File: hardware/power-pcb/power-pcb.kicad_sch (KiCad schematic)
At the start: 28 parts, among them J1 MicroFit3.0_1x2, J2 XT60PW-M-AS, J3 XT30, J4 XT30, K1 CB1-P-12V, Q1 SI4946CDY-T1-GE3, Q2 IRF4905, U1 LTC4365TS8, U2 TMCS1100A2QDR

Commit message: Added power pcb sch + design
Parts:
- removed C1, C8: 100n, Capacitor_SMD:C_0805_2012Metric_Pad1.18x1.45mm_HandSolder, symbol Device:C_Small
- removed D1: 1N4007, Diode_THT:D_DO-41_SOD81_P10.16mm_Horizontal, symbol Diode:1N4007
- removed D2: 1N4744A, Diode_THT:D_DO-41_SOD81_P10.16mm_Horizontal, symbol Diode:1N47xxA
- removed HS1: Heatsink_Pad_2Pin, Project:265118ABHE22, symbol Mechanical:Heatsink_Pad_2Pin
- removed J1: MicroFit3.0_1x2, Project:Molex_Micro-Fit_3.0_43650-0215_1x02_P3.00mm_Vertical, symbol Connector_Generic:Conn_01x02
- removed K1: CB1-P-12V, Project:CB1P12V, symbol Relay:Relay_SPDT
- removed Q1: SI4946CDY-T1-GE3, Package_SO:SO-8_3.9x4.9mm_P1.27mm, symbol Project:SISB46DN-T1-GE3
- removed Q2: IRF4905, Package_TO_SOT_THT:TO-220-3_Vertical, symbol Transistor_FET:IRF4905
- removed R2, R79: 10k, Resistor_SMD:R_0805_2012Metric_Pad1.20x1.40mm_HandSolder, symbol Device:R
- removed R6: 100R, Resistor_SMD:R_0805_2012Metric_Pad1.20x1.40mm_HandSolder, symbol Device:R_Small
- removed R88: 1.5k, Resistor_SMD:R_0805_2012Metric_Pad1.20x1.40mm_HandSolder, symbol Device:R
- removed U2: TMCS1100A2QDR, Project:TMCS1100A2QDR, symbol Project:TMCS1100A2QDR
- added C1: 2200u_LowZ, Capacitor_THT:CP_Radial_D16.0mm_P7.50mm, symbol Device:C_Polarized
- added C2: 100n, Capacitor_SMD:C_0805_2012Metric_Pad1.18x1.45mm_HandSolder, symbol Device:C_Small
- added C3, C4: 10u, Capacitor_SMD:C_0805_2012Metric_Pad1.18x1.45mm_HandSolder, symbol Device:C_Small
- added H1, H2, H3, H4: MountingHole, MountingHole:MountingHole_3.2mm_M3, symbol Mechanical:MountingHole
- added J2: XT30, Project:AMASS_XT30UPB-M_1x02_P5.0mm_Vertical, symbol Connector_Generic:Conn_01x02
- added J3: MicroFit2x12_Odd_Even, Project:Molex_Micro-Fit_3.0_43045-2412_2x12_P3.00mm_Vertical, symbol Connector_Generic:Conn_02x12_Top_Bottom
- added J4: MicroFit2x12_CouterClockwise, Project:Molex_Micro-Fit_3.0_43045-2412_2x12_P3.00mm_Vertical, symbol Connector_Generic:Conn_02x12_Counter_Clockwise
- added J7: XT60PW-M-AS, Connector_AMASS:AMASS_XT60-M_1x02_P7.20mm_Vertical, symbol Connector_Generic:Conn_01x02
- added J8: JST_XH_5, Project:JST_XH_B5B-XH-AM_1x05_P2.50mm_Vertical, symbol Connector_Generic:Conn_01x05
- added JP1: Jumper_2_Bridged, Project:TestPoint_2Pads_Pitch2.54mm_Drill0.8mm, symbol Jumper:Jumper_2_Bridged
- added Q1, Q2: SQJ138EP-T1_GE3, Project:PowerPAK_SO-8L_Single_MOS, symbol Simulation_SPICE:NMOS
- added R10, R11, R7, R9: 1k, Resistor_SMD:R_0805_2012Metric_Pad1.20x1.40mm_HandSolder, symbol Device:R
- added R16: 10k, Resistor_SMD:R_0805_2012Metric_Pad1.20x1.40mm_HandSolder, symbol Device:R
- added R6: 150, Resistor_SMD:R_0805_2012Metric_Pad1.20x1.40mm_HandSolder, symbol Device:R
- added U1: BTS50010-1TAD, Package_TO_SOT_SMD:TO-263-7_TabPin4, symbol Power_Management:BTS50010-1TAD
- added U3: R-78E3.3-1.0, Converter_DCDC:Converter_DCDC_RECOM_R-78E-0.5_THT, symbol Converter_DCDC:R-78E3.3-1.0
- D1: renamed from D3; value SMBJ18A -> SMCJ18A; footprint Diode_SMD:D_SMB_Handsoldering -> Diode_SMD:D_SMB-SMC_Universal_Handsoldering
- J1: renamed from J2; footprint Project:AMASS_XT60IPW-M_1x03_P7.20mm_Horizontal -> Connector_AMASS:AMASS_XT60-M_1x02_P7.20mm_Vertical; symbol Connector_Generic_Shielded:Conn_01x02_Shielded -> Connector_Generic:Conn_01x02
- J5: renamed from J4; footprint (none) -> Project:AMASS_XT30UPB-M_1x02_P5.0mm_Vertical; symbol Connector_Generic_Shielded:Conn_01x02_Shielded -> Connector_Generic:Conn_01x02
- J6: renamed from J3; footprint (none) -> Project:AMASS_XT30UPB-M_1x02_P5.0mm_Vertical; symbol Connector_Generic_Shielded:Conn_01x02_Shielded -> Connector_Generic:Conn_01x02
- R1: value 39R -> 10k; footprint Resistor_SMD:R_2512_6332Metric_Pad1.40x3.35mm_HandSolder -> Resistor_SMD:R_0805_2012Metric_Pad1.20x1.40mm_HandSolder
- renumbered D5 to D2, R7 to R12, R75 to R2, R13 to R8, U1 to U2
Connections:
- net BAU_UOV is gone; now on net RVP_BAU: R2.1, R3.1, U2.1 (Vin)
- net +3.3V: now also C4.1, R16.1, U3.3 (OUT)
- net +BATT: now also C3.1, J7.2 (Pin_2), U1.5 (OUT), U1.6 (OUT), U1.7 (OUT), U3.1 (IN)
- net BL.CS: now also J3.10 (Pin_10)
- net BL.D0: now also J3.8 (Pin_8)
- net BL.D1: now also J3.9 (Pin_9)
- net BL.DIR: now also J3.12 (Pin_12)
- net BL.STEP: now also J3.11 (Pin_11)
- net BR.CS: now also J3.22 (Pin_22)
- net BR.D0: now also J3.20 (Pin_20)
- net BR.D1: now also J3.21 (Pin_21)
- net BR.DIR: now also J3.24 (Pin_24)
- net BR.STEP: now also J3.23 (Pin_23)
- net FL.CS: now also J3.16 (Pin_16)
- net FL.D0: now also J3.14 (Pin_14)
- net FL.D1: now also J3.15 (Pin_15)
- net FL.DIR: now also J3.18 (Pin_18)
- net FL.STEP: now also J3.17 (Pin_17)
- net FR.CS: now also J3.4 (Pin_4)
- net FR.D0: now also J3.2 (Pin_2)
- net FR.D1: now also J3.3 (Pin_3)
- net FR.DIR: now also J3.6 (Pin_6)
- net FR.STEP: now also J3.5 (Pin_5)
- net GND: now also C1.2, C2.1, C3.2, C4.2, J3.1 (Pin_1), J3.13 (Pin_13), J3.19 (Pin_19), J3.7 (Pin_7), J4.13 (Pin_13), J4.14 (Pin_14), J4.15 (Pin_15), J4.16 (Pin_16), J4.17 (Pin_17), J4.18 (Pin_18), J4.19 (Pin_19), J4.20 (Pin_20), J4.21 (Pin_21), J4.22 (Pin_22), J4.23 (Pin_23), J4.24 (Pin_24), J7.1 (Pin_1), R6.2, U3.2 (GND); no longer J1.SH (Shield), J5.SH (Shield), J6.SH (Shield)
- net MSPI.MISO: now also J4.12 (Pin_12)
- net MSPI.MOSI: now also J4.10 (Pin_10)
- net MSPI.SCK: now also J4.11 (Pin_11)
- net PROP_EN: now also J4.9 (Pin_9), R16.2
- net RVP_BAU: now also D1.1 (K), F1.2, C2.2, Q1.1 (D); no longer R1.1
- net at R1.2: now also U1.2 (IN)
- net at U2.8 (GATE): now also Q1.2 (G), Q2.2 (G)
- net UOV_CM renamed UOV_BAU
- net UOV_BAU: now also C1.1, J2.2 (Pin_2), Q2.1 (D), U1.4 (Vbb)
- net UOV_Fault renamed UOV_FAULT
- net UOV_FAULT: now also J4.8 (Pin_8)
- new net: J8.4 (Pin_4), R11.1
- new net: R6.1, U1.1 (GND)
- new net: Q1.3 (S), Q2.3 (S)
- new net: J8.1 (Pin_1), R7.1
- new net: J8.2 (Pin_2), R9.1
- new net: J8.3 (Pin_3), R10.1
- new net: JP1.2 (B), U1.3 (IS)
- new net: J2.1 (Pin_1), R1.1
- new net BATT_C1: J4.4 (Pin_4), R11.2
- new net BATT_C2: J4.3 (Pin_3), R10.2
- new net BATT_C3: J4.2 (Pin_2), R9.2
- new net BATT_C4: J4.1 (Pin_1), R7.2
- new net ROBOT_CURRENT: J4.5 (Pin_5), JP1.1 (A)
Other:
- note added: "3.3 v"
- note added: "Cell monitoring"
- note added: "Logic PWR"
- note added: "Logic/motors"
- note added: "TVS"
- note removed: "Current Measure"
- note removed: "Reverse polarity protection + TVS"
- moved on the sheet: D1, D2, F1, R12, R2, R3, R4, R5, R8

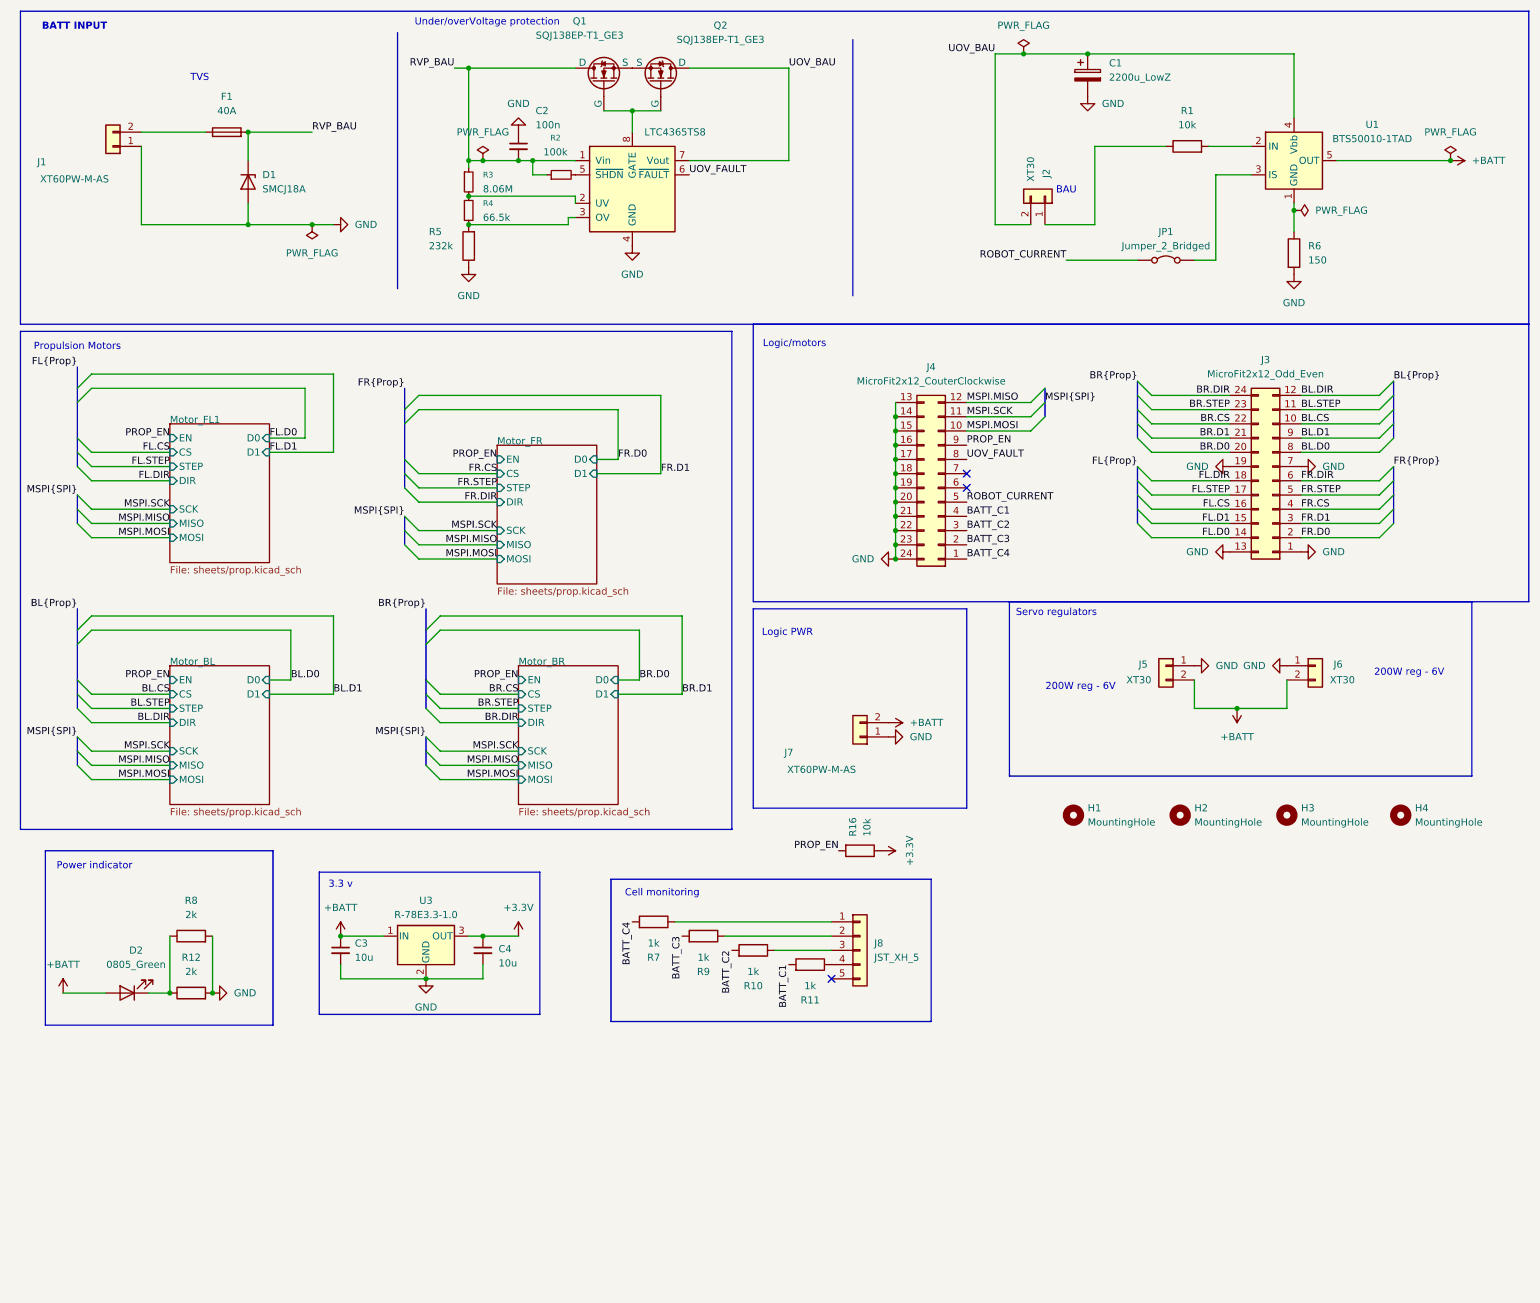
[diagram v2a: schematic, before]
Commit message: Post DRM adjustements and BOM referencing
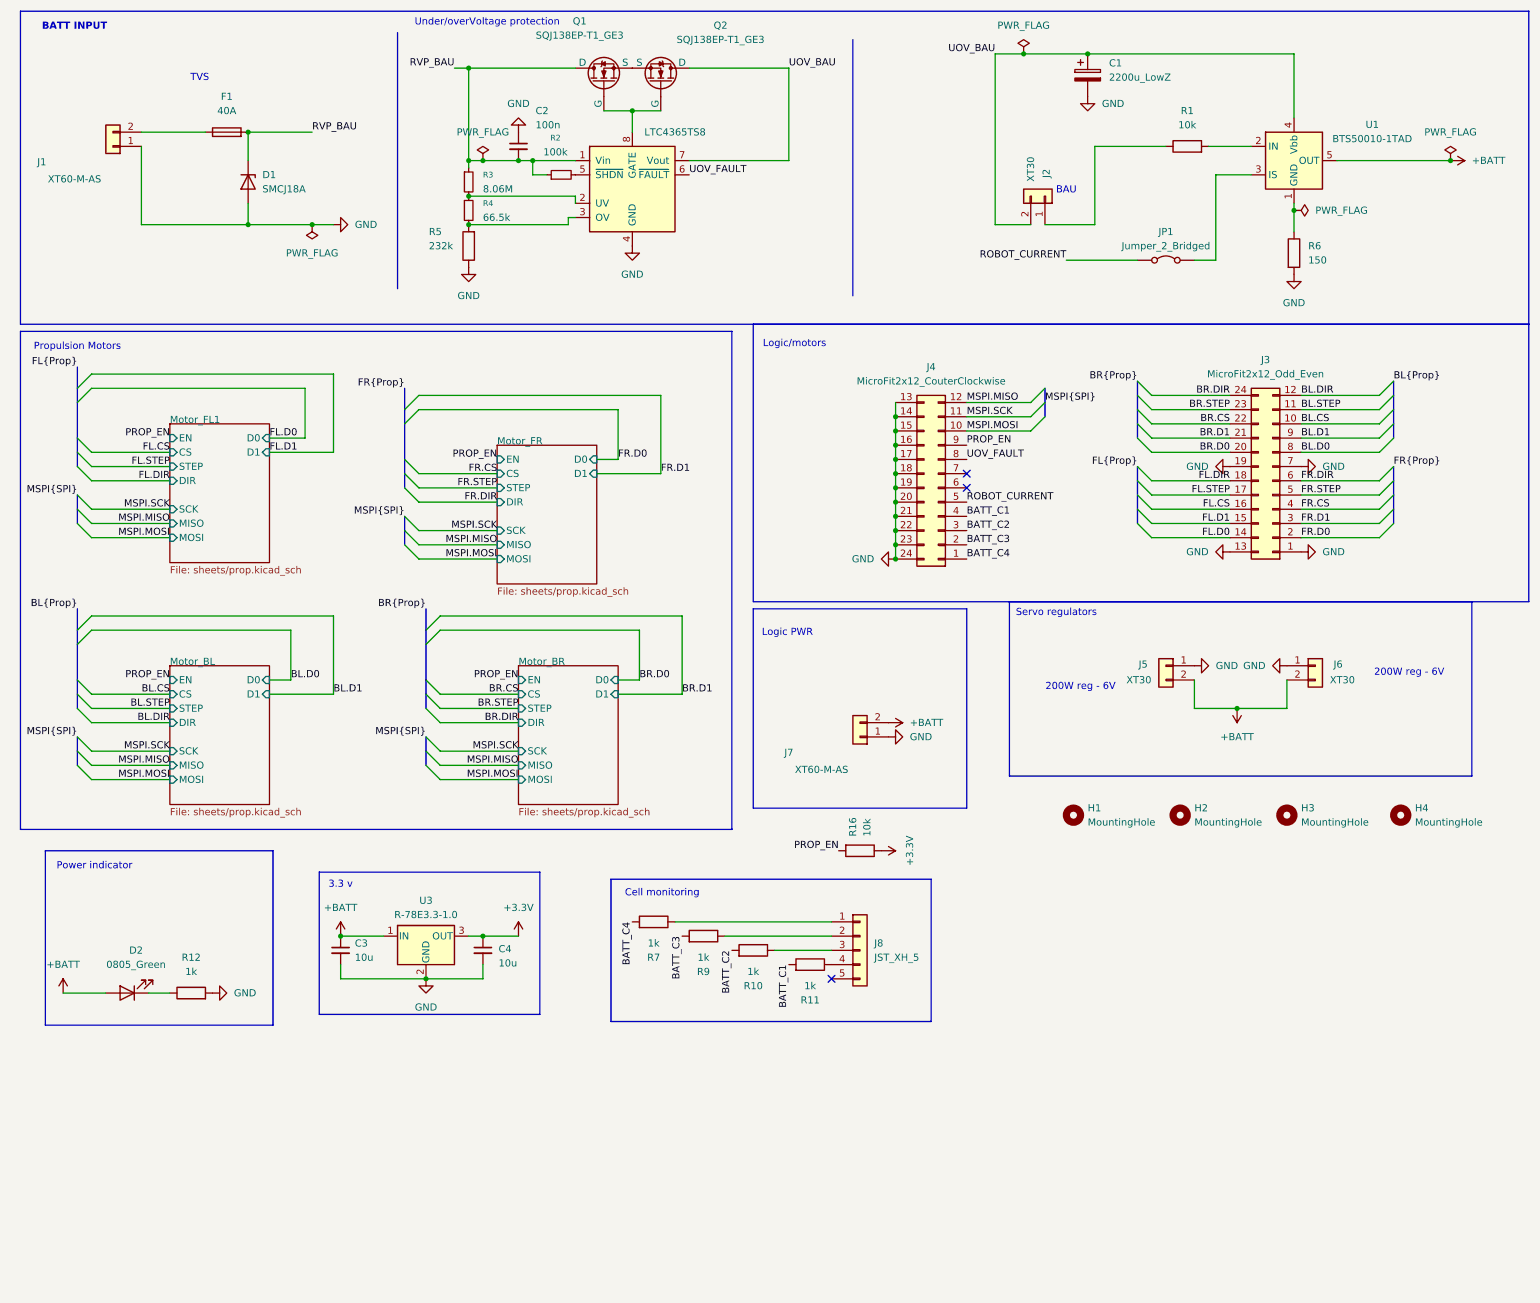
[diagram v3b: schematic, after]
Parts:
- removed R8: 2k, Resistor_SMD:R_0805_2012Metric_Pad1.20x1.40mm_HandSolder, symbol Device:R
- C1: Manufacturer (none) -> Panasonic
- C2: MPN (none) -> CL21B104KBCNNND; Manufacturer (none) -> Samsung
- C3, C4: MPN (none) -> CL21A106KBYQNNE; Manufacturer (none) -> Samsung
- D1: MPN (none) -> SMCJ18A-E3/9AT; Manufacturer (none) -> Vishay
- J1, J7: value XT60PW-M-AS -> XT60-M-AS
- J3, J4: MPN (none) -> 43045-2412; Manufacturer (none) -> Molex
- J8: MPN (none) -> B5B-XH-A-G; Manufacturer (none) -> JST
- JP1: MPN (none) -> M7582-46; Manufacturer (none) -> Harwin
- Q1, Q2: MPN (none) -> SQJ138EP-T1_GE3; Manufacturer (none) -> Vishay
- R1, R16: MPN (none) -> CRCW080510K0FKEA; Manufacturer (none) -> Vishay
- R10, R11, R7, R9: MPN (none) -> CRCW08051K00FKEA; Manufacturer (none) -> Vishay
- R12: value 2k -> 1k; MPN (none) -> CRCW08051K00FKEA; Manufacturer (none) -> Vishay
- R2: MPN (none) -> CRCW0805100KFKEA; Manufacturer (none) -> Vishay
- R3: MPN (none) -> RC0805FR-078M06L; Manufacturer (none) -> Yageo
- R4: MPN (none) -> CRCW080566K5FKEA; Manufacturer (none) -> Vishay
- R5: MPN (none) -> CRCW0805232KFKEA; Manufacturer (none) -> Vishay
- R6: MPN (none) -> CRCW0805150RFKEA; Manufacturer (none) -> Vishay
- U1: MPN (none) -> BTS500101TADATMA2; Manufacturer (none) -> Infineon
- U2: MPN (none) -> LTC4365ITS8-1#TRMPBF; Manufacturer (none) -> Analog Devices
- U3: MPN (none) -> R-78E3.3-1.0; Manufacturer (none) -> RECOM Power
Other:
- company: (none) -> Game Team SLSC
- title: (none) -> Power PCB

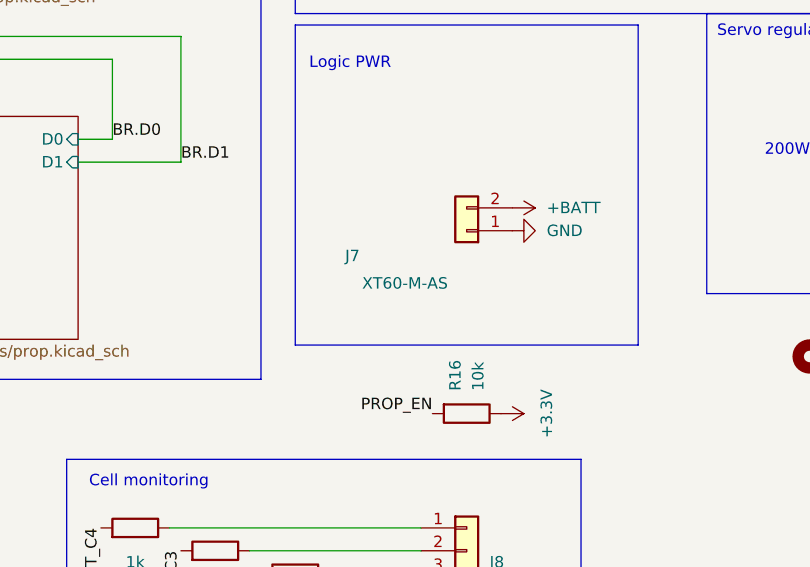
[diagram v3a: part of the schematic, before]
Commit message: Change logic connector
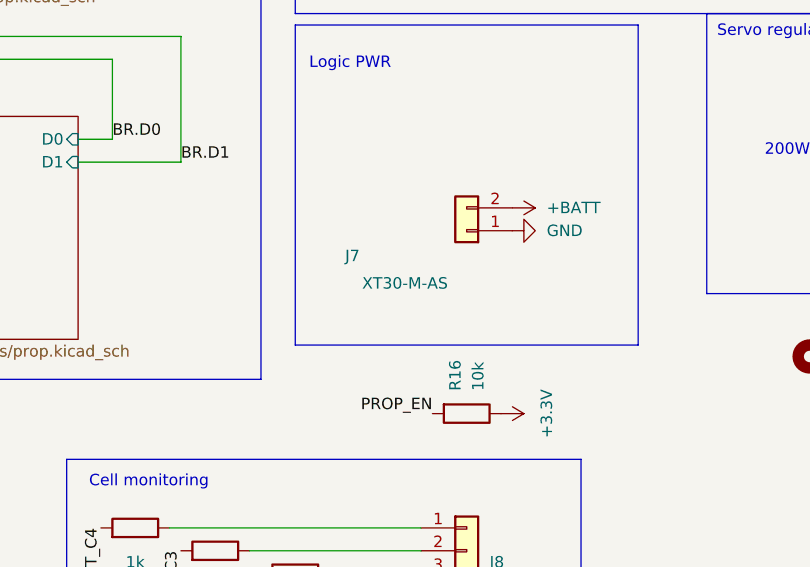
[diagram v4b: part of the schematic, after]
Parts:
- J7: value XT60-M-AS -> XT30-M-AS; footprint Connector_AMASS:AMASS_XT60-M_1x02_P7.20mm_Vertical -> Project:AMASS_XT30UPB-M_1x02_P5.0mm_Vertical
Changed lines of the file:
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@@
 			)
 		)
-		(property "Value" "XT60-M-AS"
+		(property "Value" "XT30-M-AS"
 			(at 156.972 149.352 0)
 			(effects
@@
 			)
 		)
-		(property "Footprint" "Connector_AMASS:AMASS_XT60-M_1x02_P7.20mm_Vertical"
+		(property "Footprint" "Project:AMASS_XT30UPB-M_1x02_P5.0mm_Vertical"
 			(at 163.83 143.51 0)
 			(effects

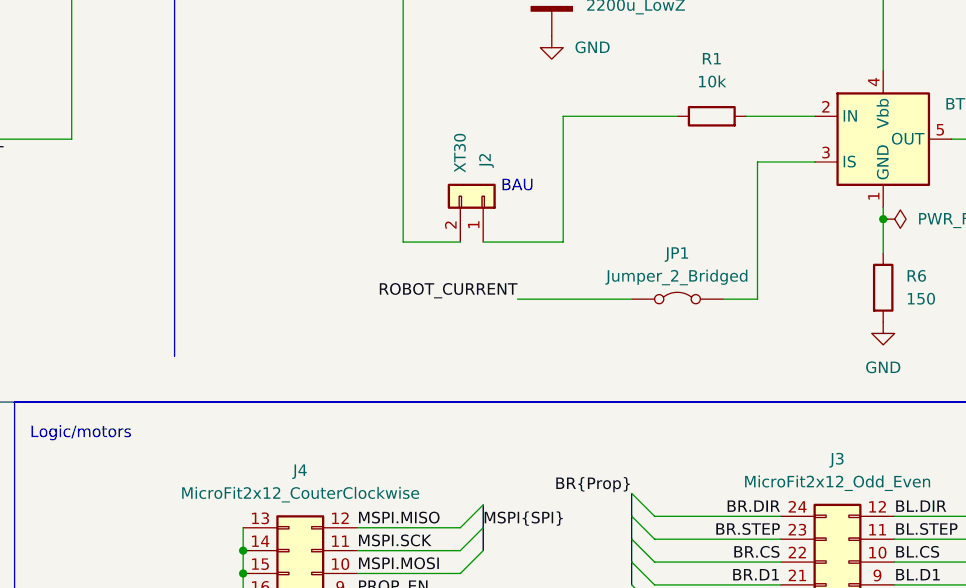
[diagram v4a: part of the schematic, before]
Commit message: Add shunt for current measure
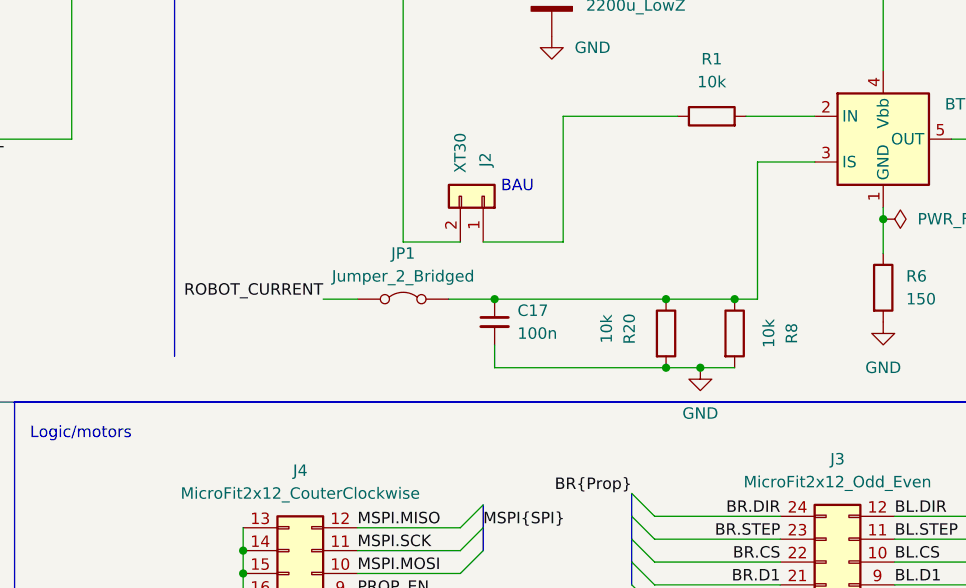
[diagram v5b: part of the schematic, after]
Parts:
- added C17: 100n, Capacitor_SMD:C_0805_2012Metric_Pad1.18x1.45mm_HandSolder, symbol Device:C_Small
- added R20, R8: 10k, Resistor_SMD:R_0805_2012Metric_Pad1.20x1.40mm_HandSolder, symbol Device:R
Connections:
- net GND: now also C17.2, R20.2, R8.2
- net at JP1.2 (B), U1.3 (IS): now also C17.1, R20.1, R8.1
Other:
- moved on the sheet: JP1

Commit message: Update README
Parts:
- C17: MPN (none) -> CL21B104KBCNNND; Manufacturer (none) -> Samsung
- R20, R8: MPN (none) -> CRCW080510K0FKEA; Manufacturer (none) -> Vishay
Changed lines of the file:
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@@
+			)
+		)
+		(property "MPN" "CRCW080510K0FKEA"
+			(at 224.79 62.23 90)
+			(effects
+				(font
+					(size 1.27 1.27)
+				)
+				(hide yes)
+			)
+		)
+		(property "Manufacturer" "Vishay"
+			(at 224.79 62.23 90)
+			(effects
+				(font
+					(size 1.27 1.27)
+				)
+				(hide yes)
 			)
 		)
@@
 			)
 		)
+		(property "MPN" "CRCW080510K0FKEA"
+			(at 217.17 62.23 90)
+			(effects
+				(font
+					(size 1.27 1.27)
+				)
+				(hide yes)
+			)
+		)
+		(property "Manufacturer" "Vishay"
+			(at 217.17 62.23 90)
+			(effects
+				(font
+					(size 1.27 1.27)
+				)
+				(hide yes)
+			)
+		)
 		(pin "2"
 		)
@@
 			(at 198.12 60.96 0)
 			(effects
+				(font
+					(size 1.27 1.27)
+				)
+				(hide yes)
+			)
+		)
+		(property "MPN" "CL21B104KBCNNND"
+			(at 198.12 60.96 0)
+			(effects
+				(font
+					(size 1.27 1.27)
+				)
+				(hide yes)
+			)
+		)
+		(property "Manufacturer" "Samsung"
+			(at 198.12 60.96 0)
+			(effects
